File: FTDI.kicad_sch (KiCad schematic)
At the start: 17 parts, among them U5 FT4232H_VQFN, Y1 Resonator_12MHz_ABM8G

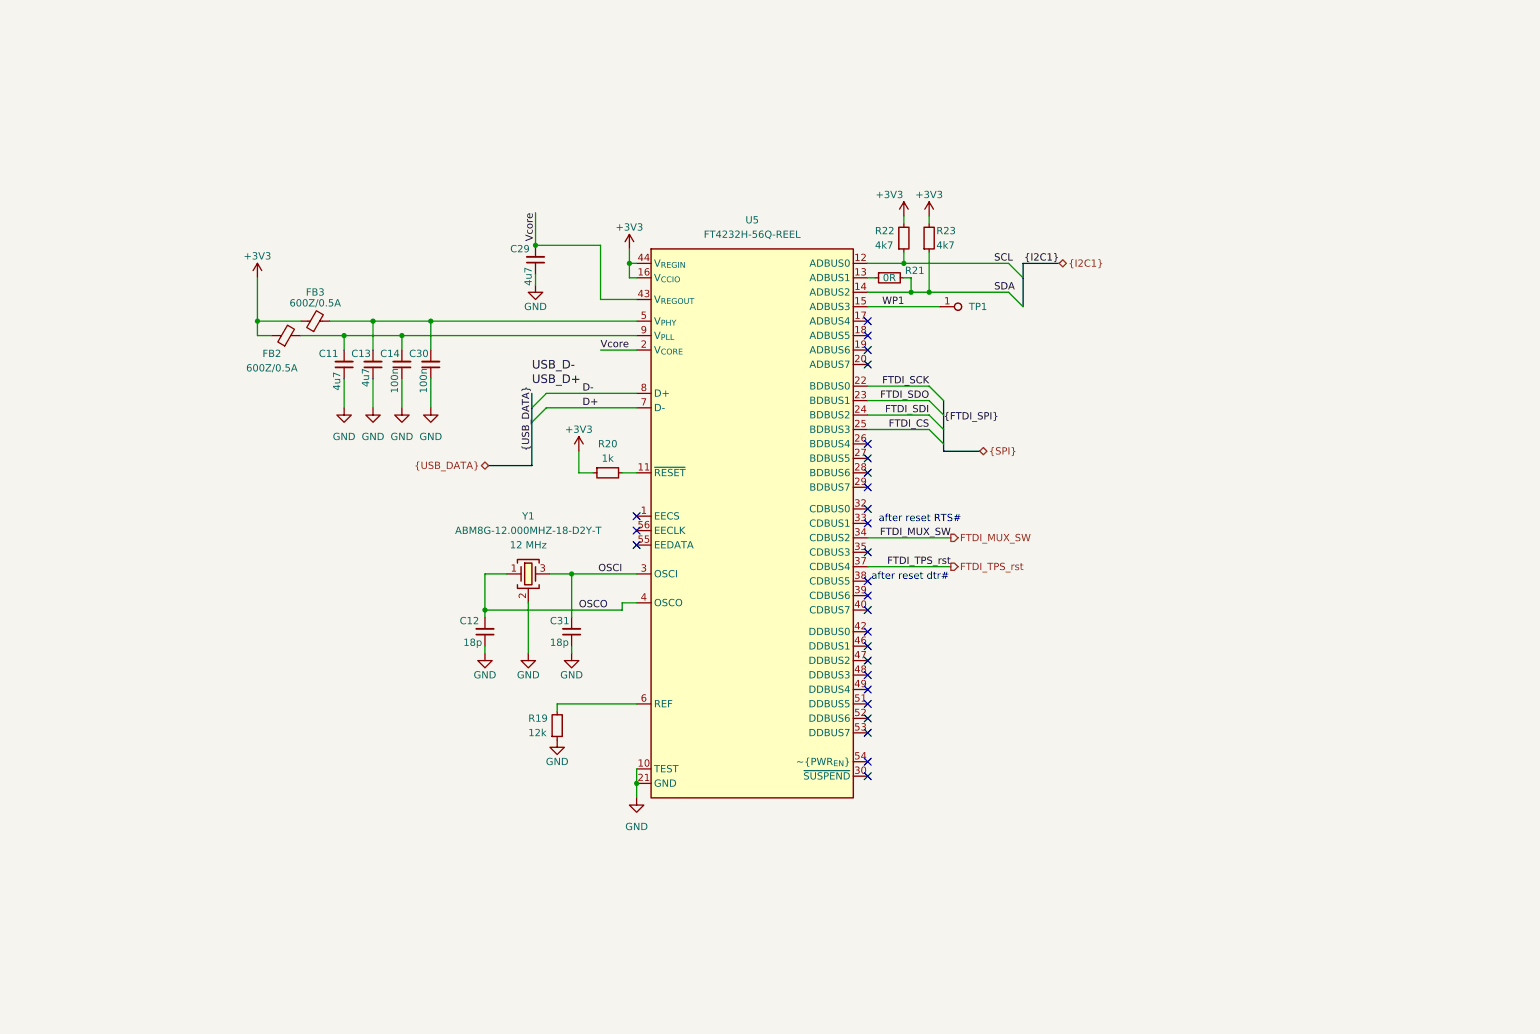
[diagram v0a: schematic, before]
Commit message: [#62623] Improve schematic, change 3V3 buck inductor, correct SPI, add testpoint
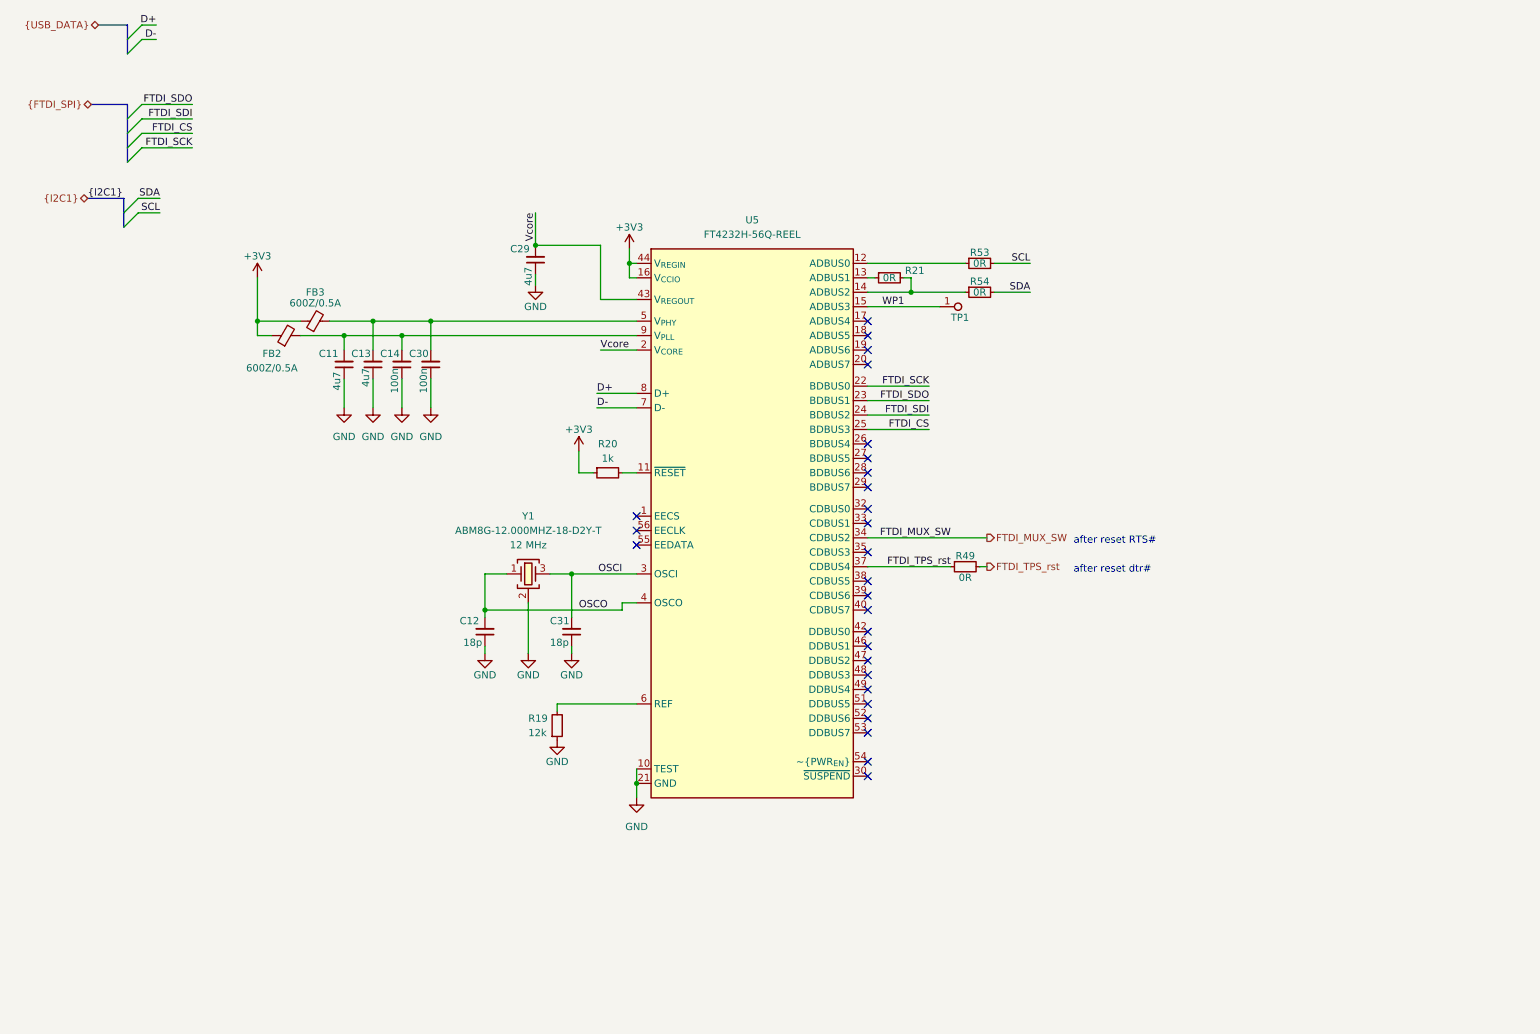
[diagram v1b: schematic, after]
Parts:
- removed R22, R23: R_4k7_0402, antmicro-footprints:R_0402_1005Metric, symbol antmicroResistors0402:R_4k7_0402
- added R49, R53, R54: R_0R_0402, antmicro-footprints:R_0402_1005Metric, symbol antmicroResistors0402:R_0R_0402
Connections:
- net D+: now also U5.8 (D+); no longer U5.7 (D-)
- net D-: now also U5.7 (D-); no longer U5.8 (D+)
- net FTDI_TPS_rst: now also R49.1, R49.2
- net SCL: now also R53.2; no longer U5.12 (ADBUS0)
- net SDA: now also R54.2; no longer R21.2, U5.14 (ADBUS2)
- new net: R21.2, R54.1, U5.14 (ADBUS2)
- new net: R53.1, U5.12 (ADBUS0)

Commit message: [#62623] Change hierarchy implementation
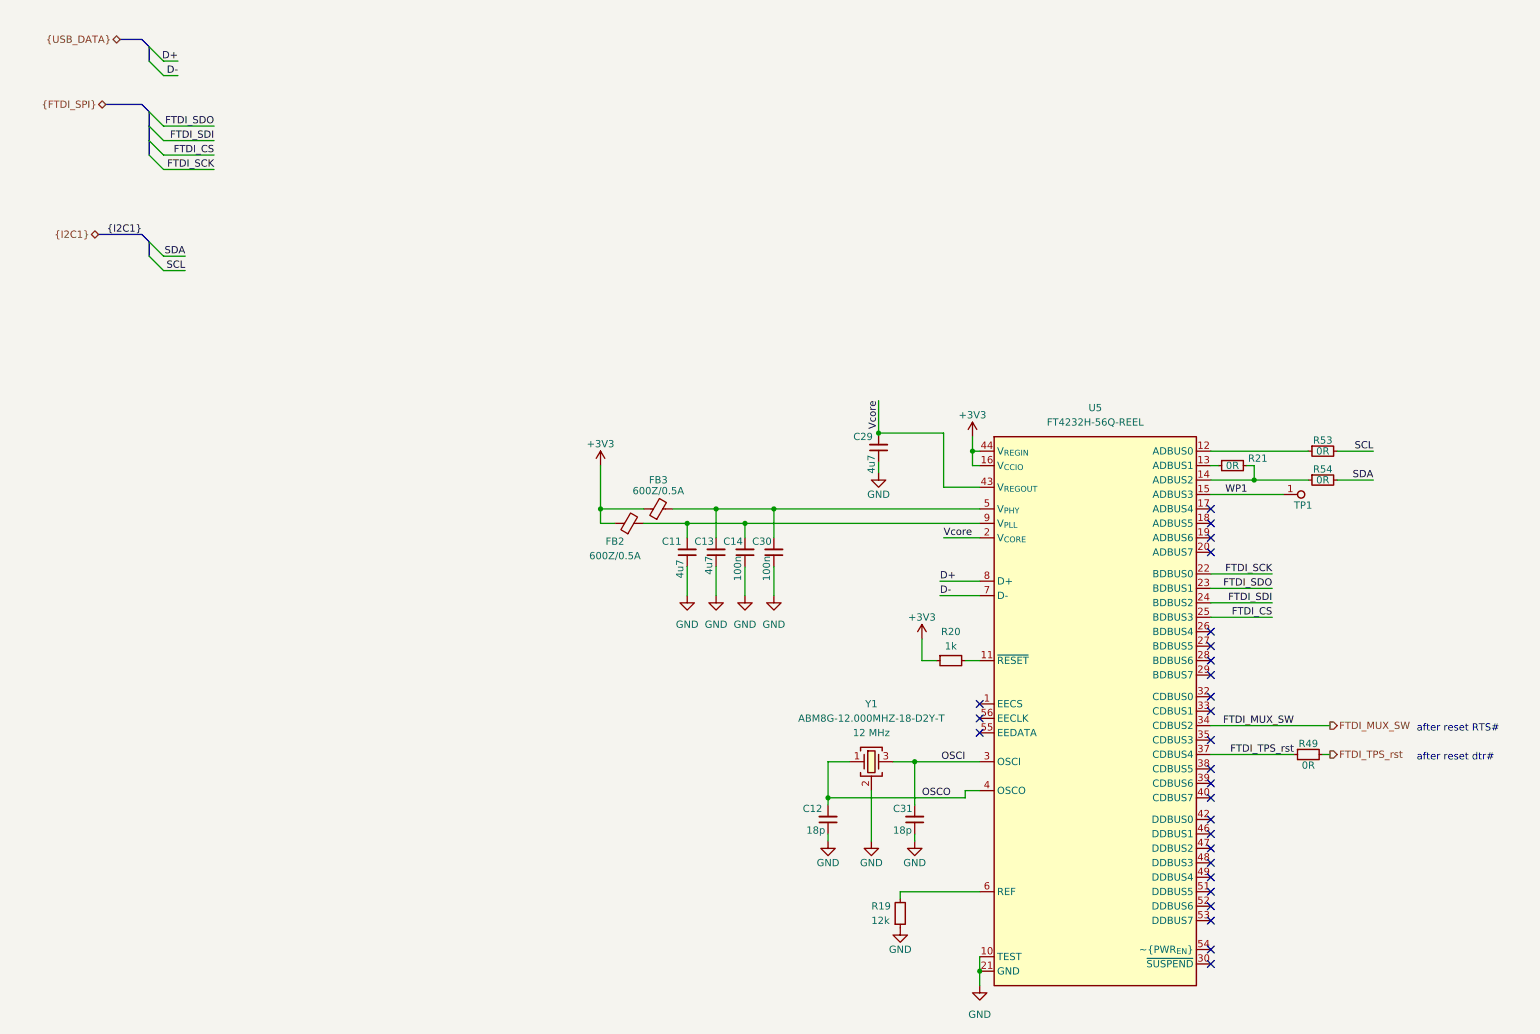
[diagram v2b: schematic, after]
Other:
- moved on the sheet: C11, C12, C13, C14, C29, C30, C31, FB2, FB3, R19, R20, R21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

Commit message: [#62623] Minor graphical changes
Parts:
- removed R49: R_0R_0402, antmicro-footprints:R_0402_1005Metric, symbol antmicroResistors0402:R_0R_0402
- added R22, R23: R_4k7_0402, antmicro-footprints:R_0402_1005Metric, symbol antmicroResistors0402:R_4k7_0402
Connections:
- net +3V3: now also R22.2, R23.2
- net at R21.2, R54.1, U5.14 (ADBUS2): now also R23.1
- net at R53.1, U5.12 (ADBUS0): now also R22.1
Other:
- moved on the sheet: R53, R54

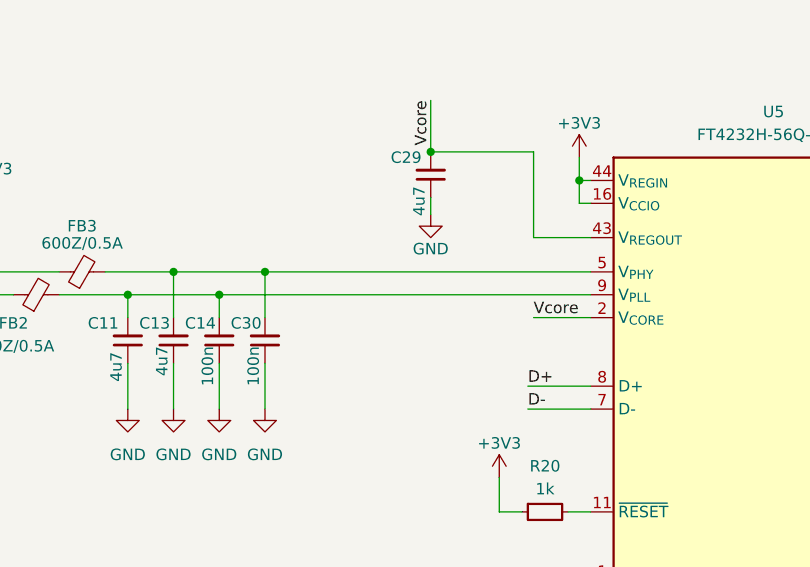
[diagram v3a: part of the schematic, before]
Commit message: [#62835] Tacle ERC problems, add PWR flags
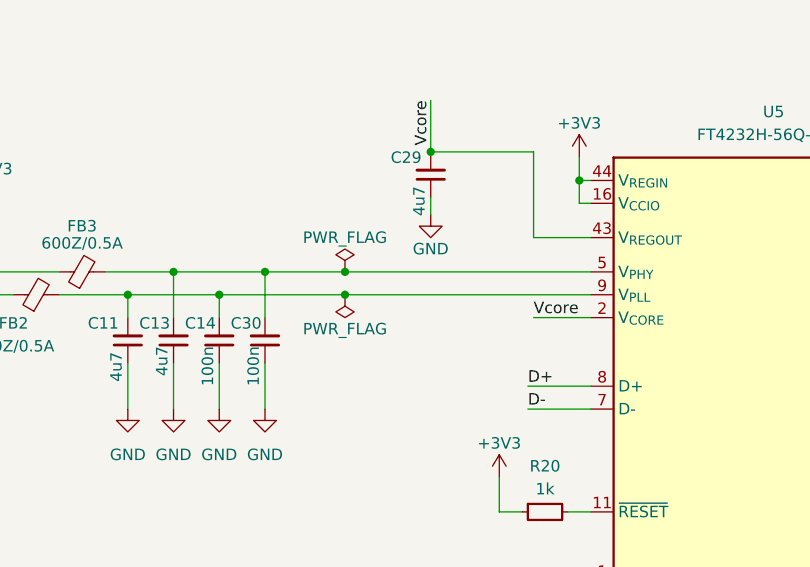
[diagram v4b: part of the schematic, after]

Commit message: [#62835] Add vias, second GND plane, GNDD plane, lower INA IC, minor changes
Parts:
- TP1: footprint antmicro-footprints:TP_SMD_1.5mm -> antmicro-footprints:TP_SMD_0.75mm
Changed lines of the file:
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@@
       (effects (font (size 1.27 1.27) (thickness 0.15)) (justify left bottom) hide)
     )
-    (property "Footprint" "antmicro-footprints:TP_SMD_1.5mm" (at 248.92 109.22 0)
+    (property "Footprint" "antmicro-footprints:TP_SMD_0.75mm" (at 248.92 109.22 0)
       (effects (font (size 1.27 1.27) (thickness 0.15)) (justify left bottom) hide)
     )

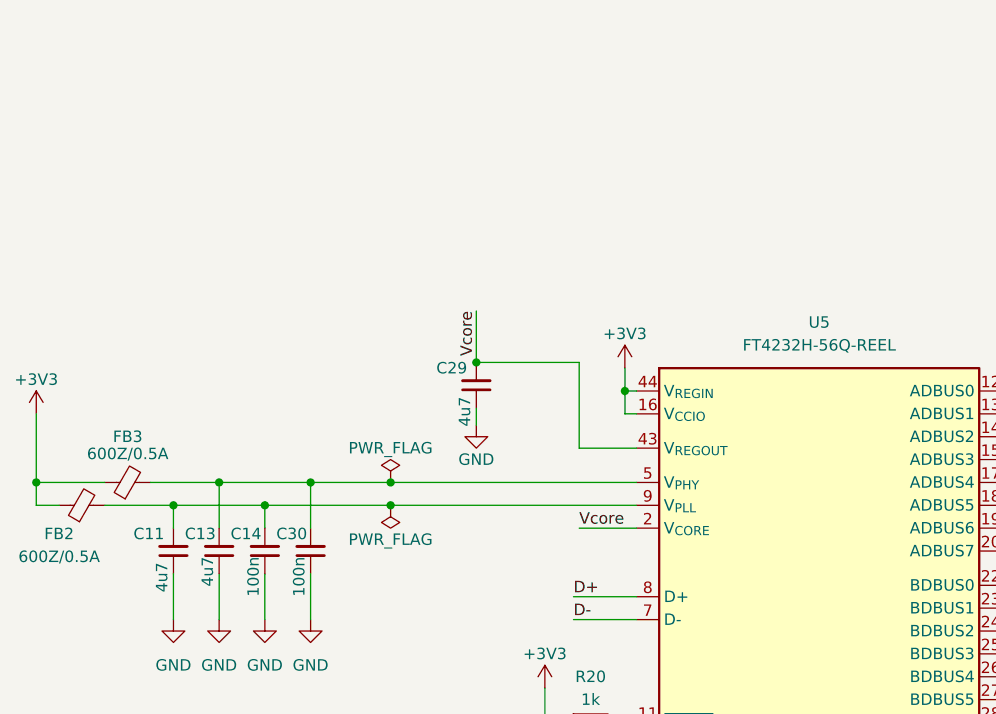
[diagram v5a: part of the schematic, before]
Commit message: [#62835] Add filtering capacitors to FTDI
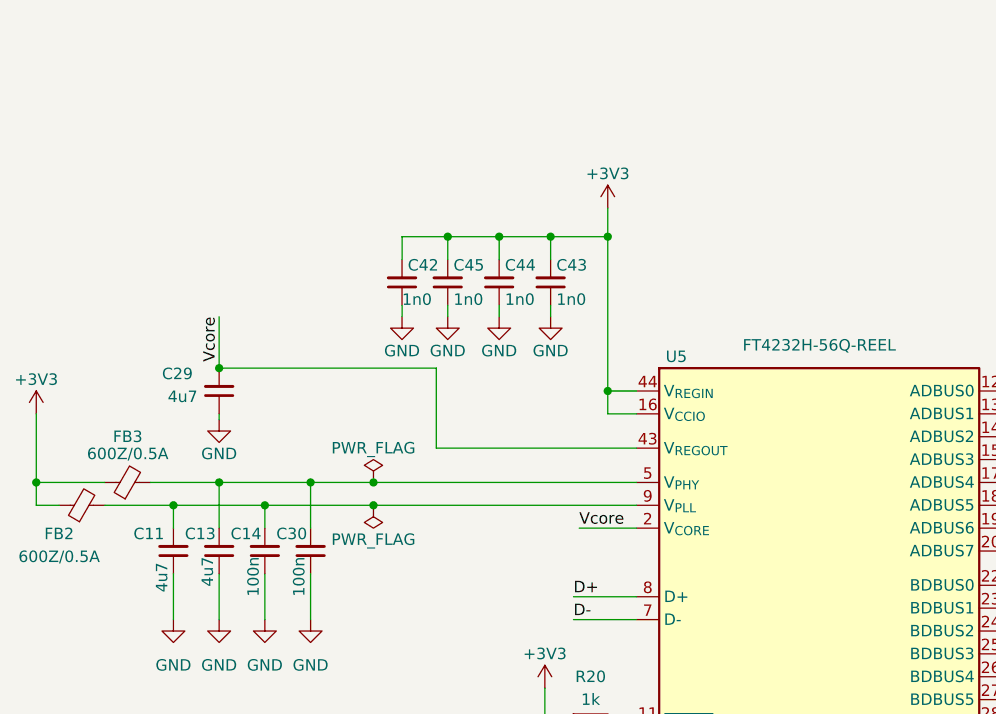
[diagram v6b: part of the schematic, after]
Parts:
- added C42, C43, C44, C45: C_1n0_0402, antmicro-footprints:C_0402_1005Metric, symbol antmicroCapacitors0402:C_1n0_0402
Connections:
- net +3V3: now also C42.2, C43.2, C44.2, C45.2
- net GND: now also C42.1, C43.1, C44.1, C45.1
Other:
- moved on the sheet: C29

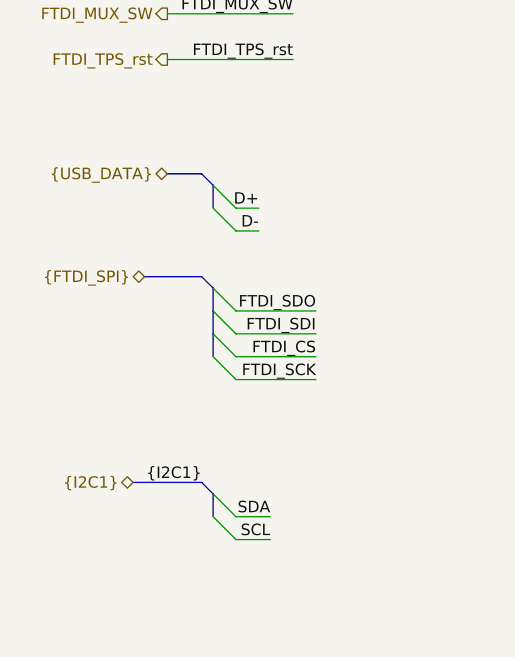
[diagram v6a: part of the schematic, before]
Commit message: [#62835] PoE to USB-C PD Review Rev.1.0.0 correct points 1,3,4,6,7,11
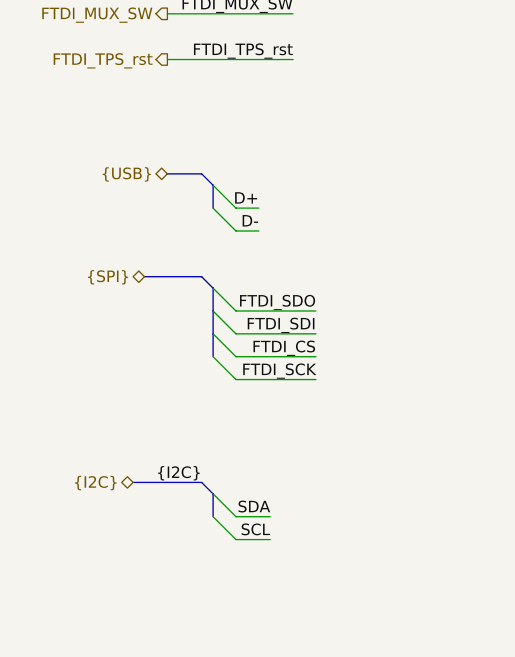
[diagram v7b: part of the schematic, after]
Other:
- company: (none) -> Antmicro ltd.
- title: (none) -> PoE to USBC PD adapter
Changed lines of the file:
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@@
 (kicad_sch (version 20230121) (generator eeschema)
   (paper "A3")
-  (bus_alias "FTDI_SPI" (members "FTDI_SDO" "FTDI_SDI" "FTDI_CS" "FTDI_SCK"))
-  (bus_alias "USB_DATA" (members "D+" "D-"))
+  (title_block
+    (title "PoE to USBC PD adapter")
+    (date "2024-07-08")
+    (company "Antmicro ltd.")
+  )
+  (bus_alias "SPI" (members "FTDI_SDO" "FTDI_SDI" "FTDI_CS" "FTDI_SCK"))
+  (bus_alias "USB" (members "D+" "D-"))
   (junction (at 133.985 88.9) (diameter 0) (color 0 0 0 0)
   )
@@
     (effects (font (size 1.27 1.27)) (justify left bottom))
   )
-  (label "{I2C1}" (at 33.02 76.2 180) (fields_autoplaced)
+  (label "{I2C}" (at 33.02 76.2 180) (fields_autoplaced)
     (effects (font (size 1.27 1.27)) (justify right bottom))
   )
@@
     (effects (font (size 1.27 1.27)) (justify right bottom))
   )
-  (hierarchical_label "{FTDI_SPI}" (shape bidirectional) (at 26.67 53.34 180) (fields_autoplaced)
+  (hierarchical_label "{SPI}" (shape bidirectional) (at 26.67 53.34 180) (fields_autoplaced)
     (effects (font (size 1.27 1.27)) (justify right))
   )
@@
     (effects (font (size 1.27 1.27)) (justify right))
   )
-  (hierarchical_label "{I2C1}" (shape bidirectional) (at 25.4 76.2 180) (fields_autoplaced)
+  (hierarchical_label "{I2C}" (shape bidirectional) (at 25.4 76.2 180) (fields_autoplaced)
     (effects (font (size 1.27 1.27)) (justify right))
   )
-  (hierarchical_label "{USB_DATA}" (shape bidirectional) (at 29.21 41.91 180) (fields_autoplaced)
+  (hierarchical_label "{USB}" (shape bidirectional) (at 29.21 41.91 180) (fields_autoplaced)
     (effects (font (size 1.27 1.27)) (justify right))
   )
